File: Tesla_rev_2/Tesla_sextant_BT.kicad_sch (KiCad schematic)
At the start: 37 parts, among them J1 Conn_01x07, J2 Conn_01x03, J3 Conn_Coaxial, J4 Conn_01x07, J5 Conn_01x03, J6 Conn_01x05, J7 Conn_01x02, J8 Conn_01x02, J9 Conn_01x02, U1 LA1185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

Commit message: revision 3
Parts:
- removed C10, C3: 39pF, Capacitor_SMD:C_0805_2012Metric_Pad1.18x1.45mm_HandSolder, symbol Device:C
- removed C11: 10nF, Capacitor_SMD:C_0805_2012Metric_Pad1.18x1.45mm_HandSolder, symbol Device:C
- removed C12, C2: 15pF, Capacitor_SMD:C_0805_2012Metric_Pad1.18x1.45mm_HandSolder, symbol Device:C
- removed C4, C5, C7: 1nF, Capacitor_SMD:C_0805_2012Metric_Pad1.18x1.45mm_HandSolder, symbol Device:C
- removed C47: 10uF, symbol Device:C_Polarized
- removed C6: 33pF, Capacitor_SMD:C_0805_2012Metric_Pad1.18x1.45mm_HandSolder, symbol Device:C
- removed C9: 100nF, Capacitor_SMD:C_0805_2012Metric_Pad1.18x1.45mm_HandSolder, symbol Device:C
- removed D1: SMAJ6.0CA, Diode_SMD:D_SMA, symbol Diode:SMAJ6.0CA
- removed FID1, FID2, FID3: Fiducial, Fiducial:Fiducial_1mm_Mask2mm, symbol Mechanical:Fiducial
- removed J1, J4: Conn_01x07, symbol Connector_Generic:Conn_01x07
- removed J2, J5: Conn_01x03, symbol Connector_Generic:Conn_01x03
- removed J3: Conn_Coaxial, symbol Connector:Conn_Coaxial
- removed J8: Conn_01x02, symbol Connector_Generic:Conn_01x02
- removed L1, L2, L3: TBD, symbol Device:L
- removed R3: 22, Resistor_SMD:R_0805_2012Metric_Pad1.20x1.40mm_HandSolder, symbol Device:R
- removed U1: LA1185, Package_SIP:SIP-9_22.3x3mm_P2.54mm, symbol RF_AM_FM:LA1185
- removed Y1: Crystal, symbol Device:Crystal
- added C36: 10uF, symbol Device:C
- added D1: PESD3V3L4UG, Package_TO_SOT_SMD:SOT-353_SC-70-5, symbol Power_Protection:PESD3V3L4UG
- added D2: ESD9B5.0ST5G, Diode_SMD:D_SOD-923, symbol Diode:ESD9B5.0ST5G
- added J2: Conn_01x06, symbol Connector_Generic:Conn_01x06
- added R26, R27: 10K, symbol Device:R
- added SW1: SW_Push, symbol Switch:SW_Push
- added U1: ESP32-C3-WROOM-02U, RF_Module:ESP32-C3-WROOM-02U, symbol RF_Module:ESP32-C3-WROOM-02U
- C1: value 6.8pF -> 10uF; footprint Capacitor_SMD:C_0805_2012Metric_Pad1.18x1.45mm_HandSolder -> (none)
- renumbered J6 to J1, J7 to J3, J9 to J4
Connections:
- net +3.3V: now also C1.1, D1.1 (K1), J2.1 (Pin_1), R26.1, R27.1, U1.1 (3V3)
- net AMP_SD: now also U1.11 (IO20/RXD)
- net AUDIO_SEL: now also U1.12 (IO21/TXD)
- net GND: now also C36.1, D1.2 (A), D2.1 (A1), J2.6 (Pin_6), SW1.2, U1.19 (GND), U1.9 (GND)
- net I2C.SCL: now also J2.3 (Pin_3), U1.7 (IO8)
- net I2C.SDA: now also J2.2 (Pin_2), U1.6 (IO7)
- net RADIO.HI: now also D1.4 (K3), U1.17 (IO1)
- net RADIO.LOW: now also D1.5 (K4), U1.15 (IO3)
- net RADIO.VOL: now also D1.3 (K2), U1.18 (IO0)
- net RADIO_AUDIO_IN: now also D2.2 (A2)
- new net EN: C36.2, SW1.1, U1.2 (EN)
- new net I2C.INT: J2.4 (Pin_4), U1.10 (IO10)
- new net I2C.~{RST}: J2.5 (Pin_5)
- new net I2S.BCK: U1.5 (IO6)
- new net I2S.DIN: U1.4 (IO5)
- new net I2S.LRCK: U1.3 (IO4)
- new net IO2: R26.2, U1.16 (IO2)
- new net IO9: R27.2, U1.8 (IO9)
- new net POWER+USB/USB_D+: U1.13 (IO18)
- new net POWER+USB/USB_D-: U1.14 (IO19)
- no-connect marks 1 -> 0
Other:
- sheet POWER renamed POWER+USB
- removed sheet IO_PANEL
- removed sheet MCU
- removed sheet USB
- added sheet freq_converter (f_conv.kicad_sch)
- sheet DAC_AMP ports: added I2S{LRCK, DIN, BCK}; removed I2S{LRCK, DIN, BCK, SCK}, XSMT
- sheet POWER+USB ports: added USB_D+, USB_D-; removed none
- note added: "15V? 5V?"
- note added: "CLC filter? Buck conv. ESP32-C3/S3 DAC Front IO FM tuner? - audio out Active frequency mixer"
- note added: "Dual-gate GaAs-FET JFET caps mix passive 2T Gilbert cell - active mix"
- note added: "FALSTAD, 1 docx"
- note added: "Front pannel conn"
- note added: "I2C, LCD, I2C to parallel"
- note added: "MT-080 AD831"
- note added: "Misc: * Schematic setup - hieary * 2 PCB 1 Project * PCB setup? 4L SGGS * PCB routing * TVS all J *"
- note added: "RC? remove?"
- note added: "Signal path, buffer, AMP?"
- note added: "SoC, Module, ANT?"
- note added: "VCO, 10MHz - 100MHz mixer Band pass"
- note added: "https://eu.mouser.com/c/passive-components/frequency-control-timing-devices/oscillators/vco-oscillators/?frequency=1.1%20MHz%20to%2025%20MHz%7C~25%20MHz%20to%2085%20MHz"
- note removed: "87,5 - 108MHz to 65,5 - 74 MHz convertor"
- note removed: "Front pannel PCB"
- moved on the sheet: H1, H2, H3, H4, J1, J3, J4, R1, R2

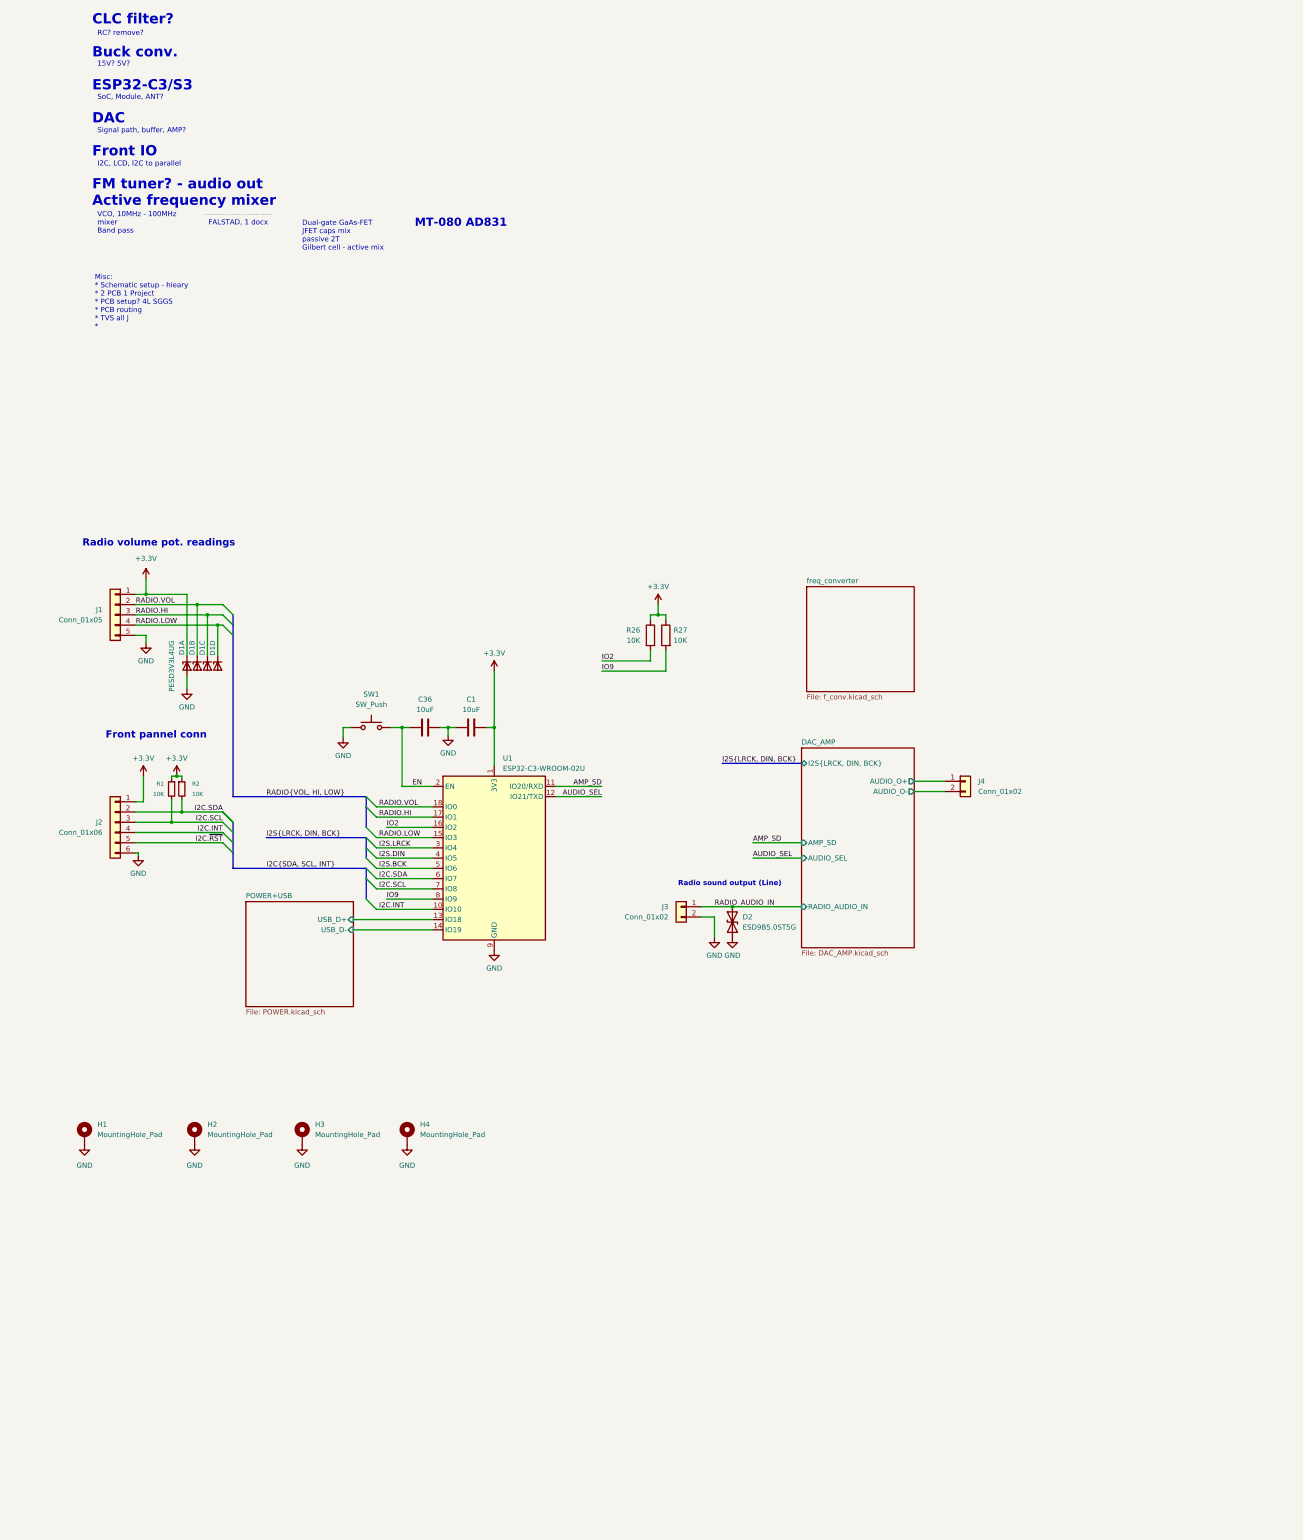
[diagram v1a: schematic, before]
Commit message: Rev 2.3, schematic and footprint fixes, prepared for layout
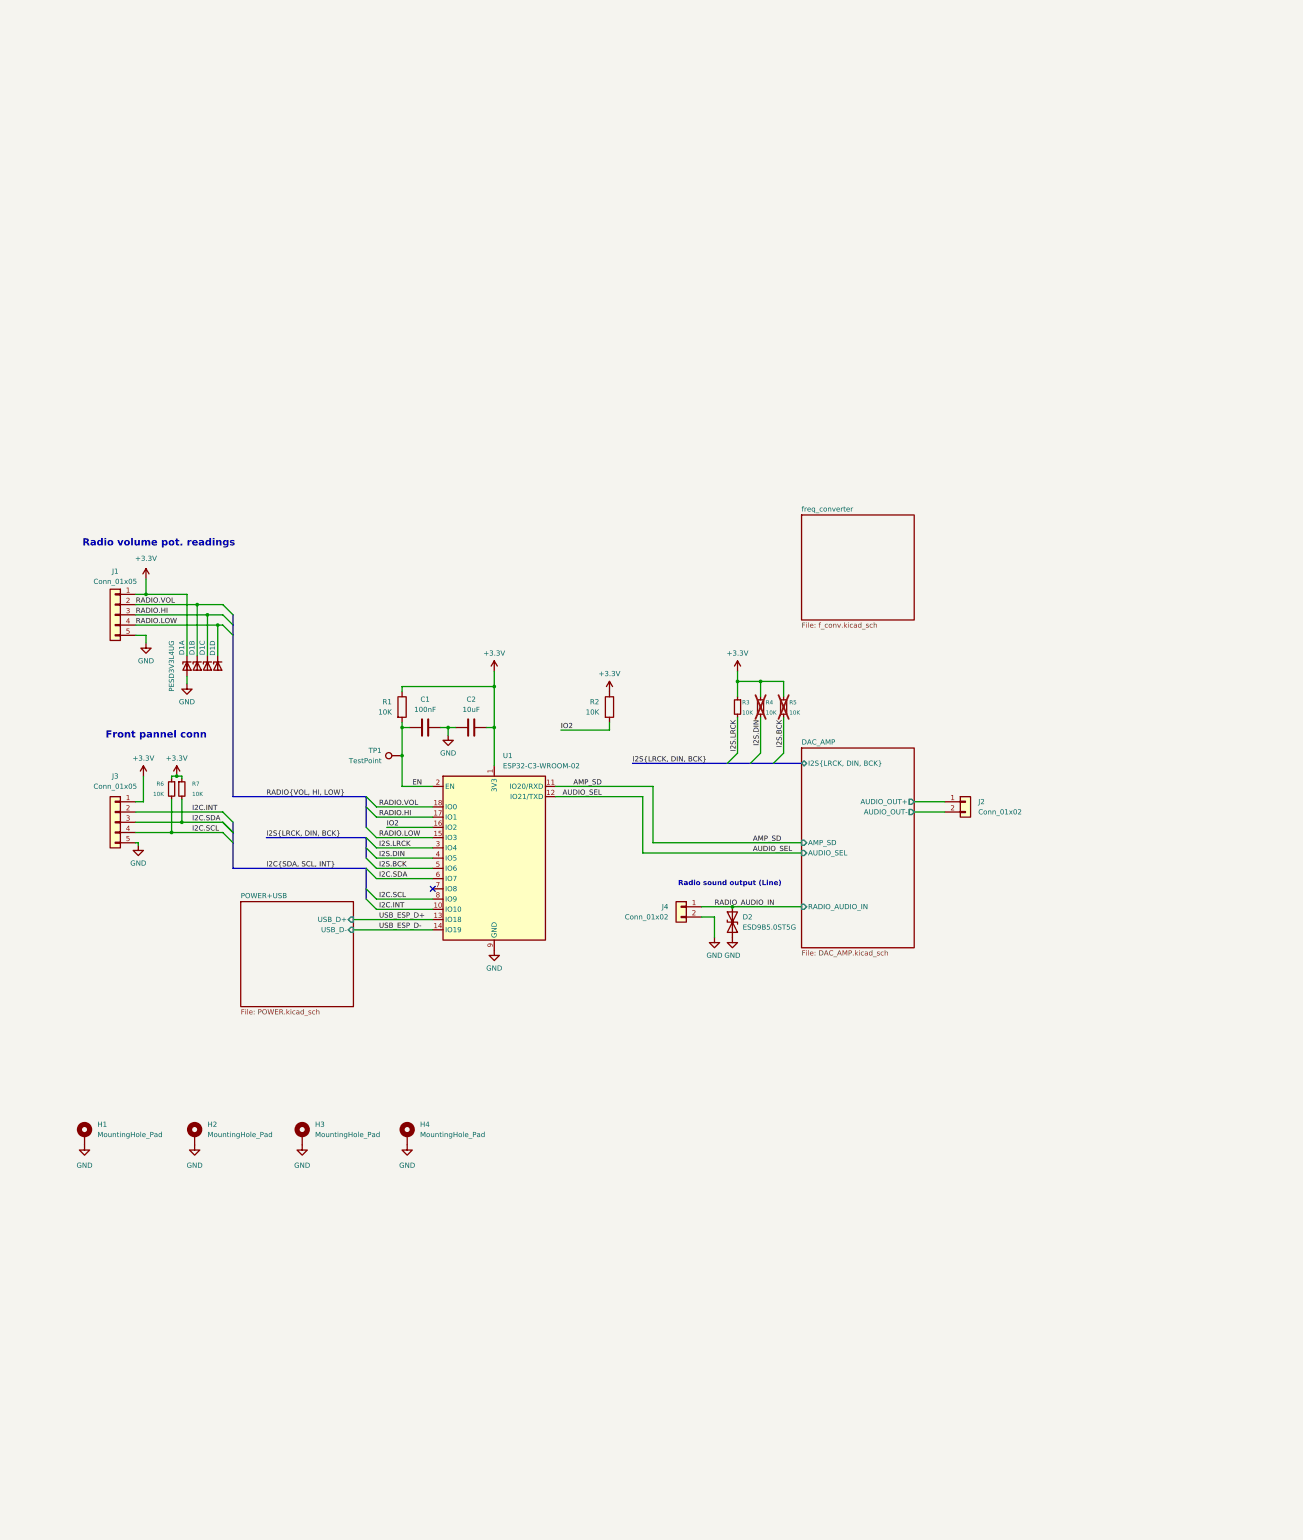
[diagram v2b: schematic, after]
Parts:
- removed J2: Conn_01x06, symbol Connector_Generic:Conn_01x06
- removed R27: 10K, symbol Device:R
- removed SW1: SW_Push, symbol Switch:SW_Push
- removed U1: ESP32-C3-WROOM-02U, RF_Module:ESP32-C3-WROOM-02U, symbol RF_Module:ESP32-C3-WROOM-02U
- added J3: Conn_01x05, Connector_PinSocket_2.00mm:PinSocket_1x05_P2.00mm_Vertical, symbol Connector_Generic:Conn_01x05
- added R1: 10K, Capacitor_SMD:C_0805_2012Metric, symbol Device:R
- added R3, R4, R5: 10K, Capacitor_SMD:C_0805_2012Metric, symbol Device:R_Small
- added TP1: TestPoint, TestPoint:TestPoint_Pad_D2.5mm, symbol Connector:TestPoint
- added U1: ESP32-C3-WROOM-02, RF_Module:ESP32-C3-WROOM-02, symbol RF_Module:ESP32-C3-WROOM-02
- C1: renamed from C36; value 10uF -> 100nF; footprint (none) -> Capacitor_SMD:C_0805_2012Metric
- C2: renamed from C1; footprint (none) -> Capacitor_SMD:C_0805_2012Metric
- H1, H2, H3, H4: footprint (none) -> MountingHole:MountingHole_4.3mm_M4_DIN965_Pad_TopBottom
- J1: footprint (none) -> Connector_PinSocket_2.00mm:PinSocket_1x05_P2.00mm_Vertical
- J2: renamed from J4; footprint (none) -> Tesla_Library:Conn_Solder_1x02_SMD; now left out of the parts list
- J4: renamed from J3; footprint (none) -> Tesla_Library:Conn_Solder_1x02_SMD; now left out of the parts list
- R2: renamed from R26; footprint (none) -> Capacitor_SMD:C_0805_2012Metric
- R6: renamed from R1; footprint (none) -> Capacitor_SMD:C_0805_2012Metric
- R7: renamed from R2; footprint (none) -> Capacitor_SMD:C_0805_2012Metric
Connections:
- net +3.3V: now also J3.1 (Pin_1), R1.1, R3.1, R4.1, R5.1, U1.1 (3V3)
- net AMP_SD: now also U1.11 (IO20/RXD)
- net AUDIO_SEL: now also U1.12 (IO21/TXD)
- net EN: now also R1.2, TP1.1, U1.2 (EN)
- net GND: now also J3.5 (Pin_5), U1.19 (GND), U1.9 (GND)
- net I2C.INT: now also J3.2 (Pin_2), U1.10 (IO10)
- net I2C.SCL: now also J3.4 (Pin_4), U1.8 (IO9)
- net I2C.SDA: now also J3.3 (Pin_3), U1.6 (IO7)
- net I2S.BCK: now also R5.2, U1.5 (IO6)
- net I2S.DIN: now also R4.2, U1.4 (IO5)
- net I2S.LRCK: now also R3.2, U1.3 (IO4)
- net IO2: now also U1.16 (IO2)
- net RADIO.HI: now also U1.17 (IO1)
- net RADIO.LOW: now also U1.15 (IO3)
- net RADIO.VOL: now also U1.18 (IO0)
- net DAC_AMP/AUDIO_O+ renamed DAC_AMP/AUDIO_OUT+
- net DAC_AMP/AUDIO_O- renamed DAC_AMP/AUDIO_OUT-
- new net USB_ESP_D+: U1.13 (IO18)
- new net USB_ESP_D-: U1.14 (IO19)
- no-connect marks 0 -> 1
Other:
- sheet DAC_AMP ports: added AUDIO_OUT+, AUDIO_OUT-; removed AUDIO_O+, AUDIO_O-
- note removed: "15V? 5V?"
- note removed: "CLC filter? Buck conv. ESP32-C3/S3 DAC Front IO FM tuner? - audio out Active frequency mixer"
- note removed: "Dual-gate GaAs-FET JFET caps mix passive 2T Gilbert cell - active mix"
- note removed: "FALSTAD, 1 docx"
- note removed: "I2C, LCD, I2C to parallel"
- note removed: "MT-080 AD831"
- note removed: "Misc: * Schematic setup - hieary * 2 PCB 1 Project * PCB setup? 4L SGGS * PCB routing * TVS all J *"
- note removed: "RC? remove?"
- note removed: "Signal path, buffer, AMP?"
- note removed: "SoC, Module, ANT?"
- note removed: "VCO, 10MHz - 100MHz mixer Band pass"
- note removed: "https://eu.mouser.com/c/passive-components/frequency-control-timing-devices/oscillators/vco-oscillators/?frequency=1.1%20MHz%20to%2025%20MHz%7C~25%20MHz%20to%2085%20MHz"
- moved on the sheet: J2, R2

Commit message: added PCB layou
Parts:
- removed D1: PESD3V3L4UG, Package_TO_SOT_SMD:SOT-353_SC-70-5, symbol Power_Protection:PESD3V3L4UG
- removed D2: ESD9B5.0ST5G, Diode_SMD:D_SOD-923, symbol Diode:ESD9B5.0ST5G
- added D1: WE-TVS-824015043, Package_TO_SOT_SMD:SOT-23-6, symbol Power_Protection:WE-TVS-824015043
- added D2: SMAJ5.0CA, Diode_SMD:D_SMA, symbol Diode:SMAJ5.0CA
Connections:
- net +3.3V: now also D1.5 (VBUS)
- net AMP_SD: now also U1.12 (IO21/TXD); no longer U1.11 (IO20/RXD)
- net AUDIO_SEL: now also U1.11 (IO20/RXD); no longer U1.12 (IO21/TXD)
- net GND: now also D1.2 (GND), D2.2 (A2)
- net I2C.INT: now also J3.4 (Pin_4); no longer J3.2 (Pin_2)
- net I2C.SCL: now also J3.3 (Pin_3); no longer J3.4 (Pin_4)
- net I2C.SDA: now also J3.2 (Pin_2); no longer J3.3 (Pin_3)
- net I2S.BCK: now also U1.3 (IO4); no longer U1.5 (IO6)
- net I2S.LRCK: now also U1.5 (IO6); no longer U1.3 (IO4)
- net RADIO.HI: now also D1.3 (I/O2)
- net RADIO.LOW: now also J1.2 (Pin_2), D1.4 (I/O3); no longer J1.4 (Pin_4)
- net RADIO.VOL: now also J1.4 (Pin_4), D1.1 (I/O1); no longer J1.2 (Pin_2)
- net RADIO_AUDIO_IN: now also D2.1 (A1)
- no-connect marks 1 -> 2
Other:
- sheet DAC_AMP ports: added INPUT_SEL; removed AUDIO_SEL
